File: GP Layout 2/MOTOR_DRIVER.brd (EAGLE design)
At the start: 91.4 x 97.5 mm, 82 parts, among them T1 2N2222, T2 2N2222, U7 ATMEGA328P_TQFP, Y1 16MHz

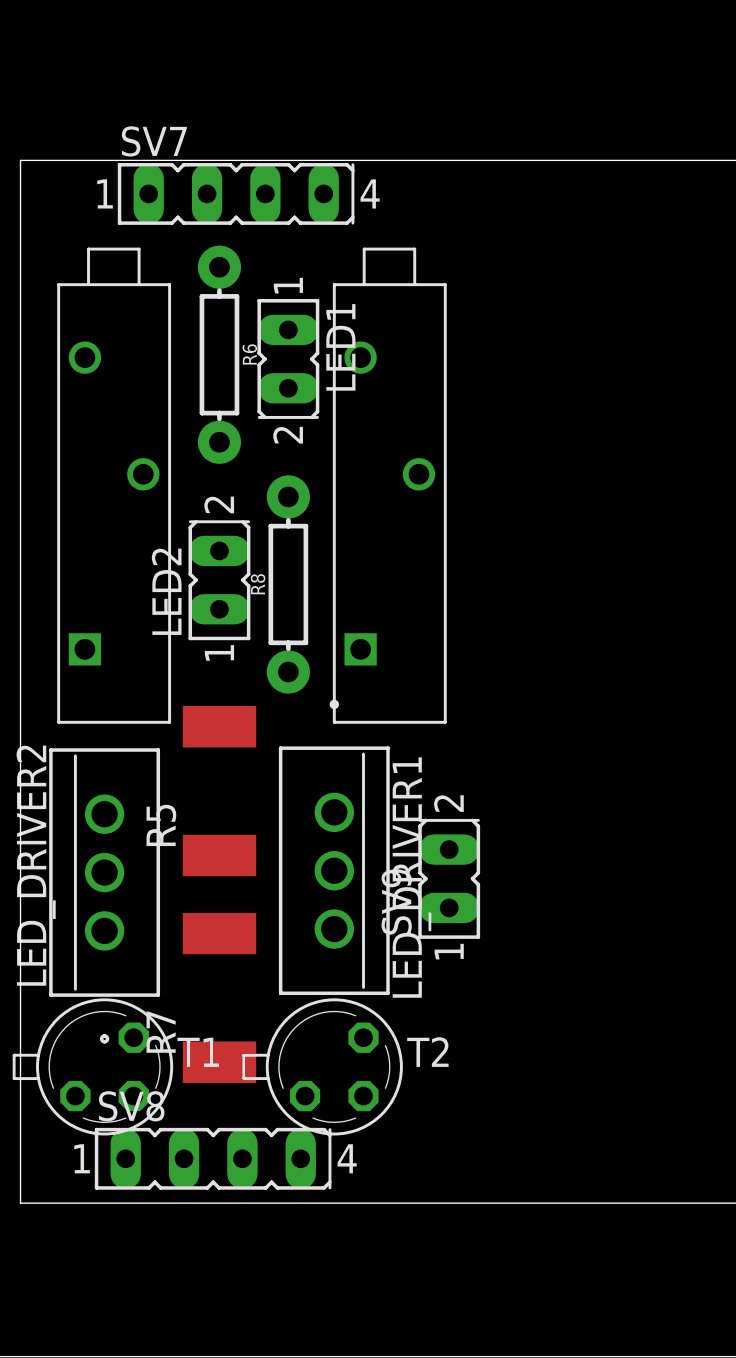
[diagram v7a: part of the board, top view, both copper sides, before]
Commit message: added actual LEDs
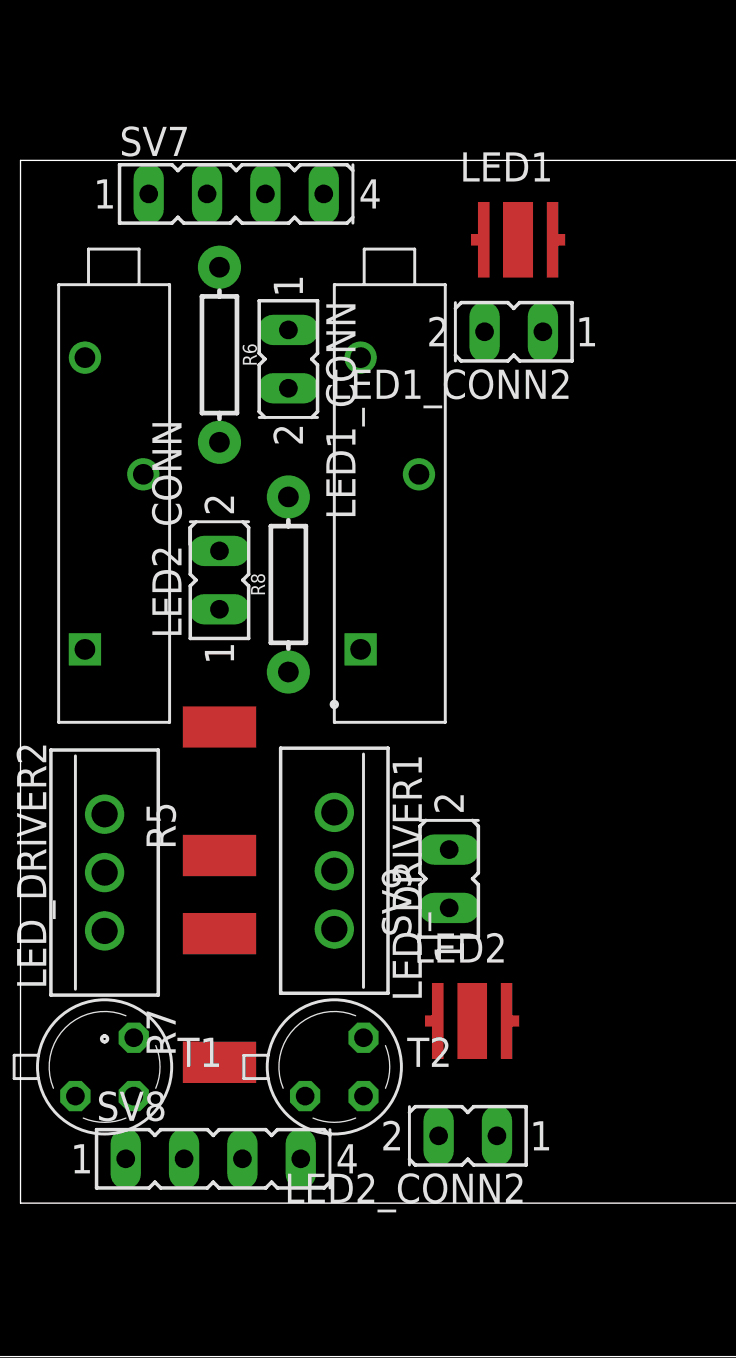
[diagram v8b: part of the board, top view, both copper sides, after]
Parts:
- added LED1_CONN, LED1_CONN2, LED2_CONN, LED2_CONN2: (no value), con-lsta:FE02-1
- LED1, LED2: value (none) -> CREE_XP; device con-lsta:FE02-1 -> Cree_XP:XP
- moved LED2 25.5 mm to (73.0, 60.0), turned to 0 degrees
- moved LED1 13.5 mm to (75.0, 94.0), turned to 0 degrees
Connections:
- new net LED1HI: LED1.POSITIVE, LED1.POSITIVE1, LED1_CONN2.2
- new net LED1LO: LED1.NEGATIVE, LED1.NEGATIVE1, LED1_CONN2.1
- new net LED2HI: LED2.POSITIVE, LED2.POSITIVE1, LED2_CONN2.2
- new net LED2LO: LED2.NEGATIVE, LED2.NEGATIVE1, LED2_CONN2.1
- net 7_4V_TOP2: now also LED1_CONN.2, LED2_CONN.2; no longer LED1.2, LED2.2
- net N$17: now also LED1_CONN.1; no longer LED1.1
- net N$20: now also LED2_CONN.1; no longer LED2.1
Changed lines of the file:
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@@
 <element name="SV7" library="con-lsta" package="FE04-1" value="" x="64" y="96"/>
 <element name="SV8" library="con-lsta" package="FE04-1" value="" x="63" y="54"/>
-<element name="LED1" library="con-lsta" package="FE02-1" value="" x="65" y="85" rot="R270"/>
-<element name="LED2" library="con-lsta" package="FE02-1" value="" x="62" y="83" rot="R90"/>
+<element name="LED1_CONN" library="con-lsta" package="FE02-1" value="" x="65" y="85" rot="R270"/>
+<element name="LED2_CONN" library="con-lsta" package="FE02-1" value="" x="62" y="83" rot="R90"/>
 <element name="SV9" library="con-lsta" package="FE02-1" value="" x="72" y="70" rot="R90"/>
 <element name="U$8" library="heatsink" package="HEATSINK" value="" x="46" y="44" rot="R180"/>
@@
 <element name="D5" library="SparkFun-LED" package="LED-0603" value="" x="6" y="10" rot="R180"/>
 <element name="TXRX" library="con-lsta" package="FE02-1" value="" x="71" y="30"/>
+<element name="LED1" library="Cree_XP" package="XP" value="CREE_XP" x="75" y="94"/>
+<element name="LED2" library="Cree_XP" package="XP" value="CREE_XP" x="73" y="60"/>
+<element name="LED1_CONN2" library="con-lsta" package="FE02-1" value="" x="71" y="90" rot="R180"/>
+<element name="LED2_CONN2" library="con-lsta" package="FE02-1" value="" x="69" y="55" rot="R180"/>
 </elements>
 <signals>
@@
 <signal name="N$17">
 <contactref element="LED_DRIVER2" pad="2"/>
-<contactref element="LED1" pad="1"/>
+<contactref element="LED1_CONN" pad="1"/>
 <wire x1="65" y1="90.08" x2="57" y2="66.46" width="0" layer="19" extent="1-1"/>
 </signal>
@@
 <signal name="N$20">
 <contactref element="LED_DRIVER1" pad="2"/>
-<contactref element="LED2" pad="1"/>
+<contactref element="LED2_CONN" pad="1"/>
 <wire x1="62" y1="77.92" x2="67" y2="66.54" width="0" layer="19" extent="1-1"/>
 </signal>
@@
 <contactref element="R6" pad="P$2"/>
 <contactref element="R8" pad="P$2"/>
-<contactref element="LED1" pad="2"/>
-<contactref element="LED2" pad="2"/>
+<contactref element="LED1_CONN" pad="2"/>
+<contactref element="LED2_CONN" pad="2"/>
 <contactref element="SV9" pad="2"/>
 <wire x1="62" y1="85.19" x2="65" y2="87.54" width="0" layer="19" extent="1-1"/>
@@
 <wire x1="10.05" y1="24" x2="6.877" y2="10" width="0" layer="19" extent="1-1"/>
 </signal>
+<signal name="LED1HI">
+<contactref element="LED1" pad="POSITIVE"/>
+<contactref element="LED1" pad="POSITIVE1"/>
+<contactref element="LED1_CONN2" pad="2"/>
+<wire x1="73.5" y1="94" x2="73.54" y2="90" width="0" layer="19" extent="1-1"/>
+<wire x1="73.15" y1="94" x2="73.5" y2="94" width="0" layer="19" extent="1-1"/>
+</signal>
+<signal name="LED1LO">
+<contactref element="LED1" pad="NEGATIVE"/>
+<contactref element="LED1" pad="NEGATIVE1"/>
+<contactref element="LED1_CONN2" pad="1"/>
+<wire x1="76.5" y1="94" x2="76.08" y2="90" width="0" layer="19" extent="1-1"/>
+<wire x1="76.85" y1="94" x2="76.5" y2="94" width="0" layer="19" extent="1-1"/>
+</signal>
+<signal name="LED2HI">
+<contactref element="LED2" pad="POSITIVE"/>
+<contactref element="LED2" pad="POSITIVE1"/>
+<contactref element="LED2_CONN2" pad="2"/>
+<wire x1="71.5" y1="60" x2="71.54" y2="55" width="0" layer="19" extent="1-1"/>
+<wire x1="71.15" y1="60" x2="71.5" y2="60" width="0" layer="19" extent="1-1"/>
+</signal>
+<signal name="LED2LO">
+<contactref element="LED2" pad="NEGATIVE"/>
+<contactref element="LED2" pad="NEGATIVE1"/>
+<contactref element="LED2_CONN2" pad="1"/>
+<wire x1="74.85" y1="60" x2="74.08" y2="55" width="0" layer="19" extent="1-1"/>
+<wire x1="74.5" y1="60" x2="74.85" y2="60" width="0" layer="19" extent="1-1"/>
+</signal>
 </signals>
